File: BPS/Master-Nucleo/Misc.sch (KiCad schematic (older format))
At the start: 34 parts, among them J11 FrontFans, J12 BackFans, J13 ErrorLightConnector, Q3 NTR4003NT1G, Q4 NTR4003NT1G, U16 SI8261ABC-IS

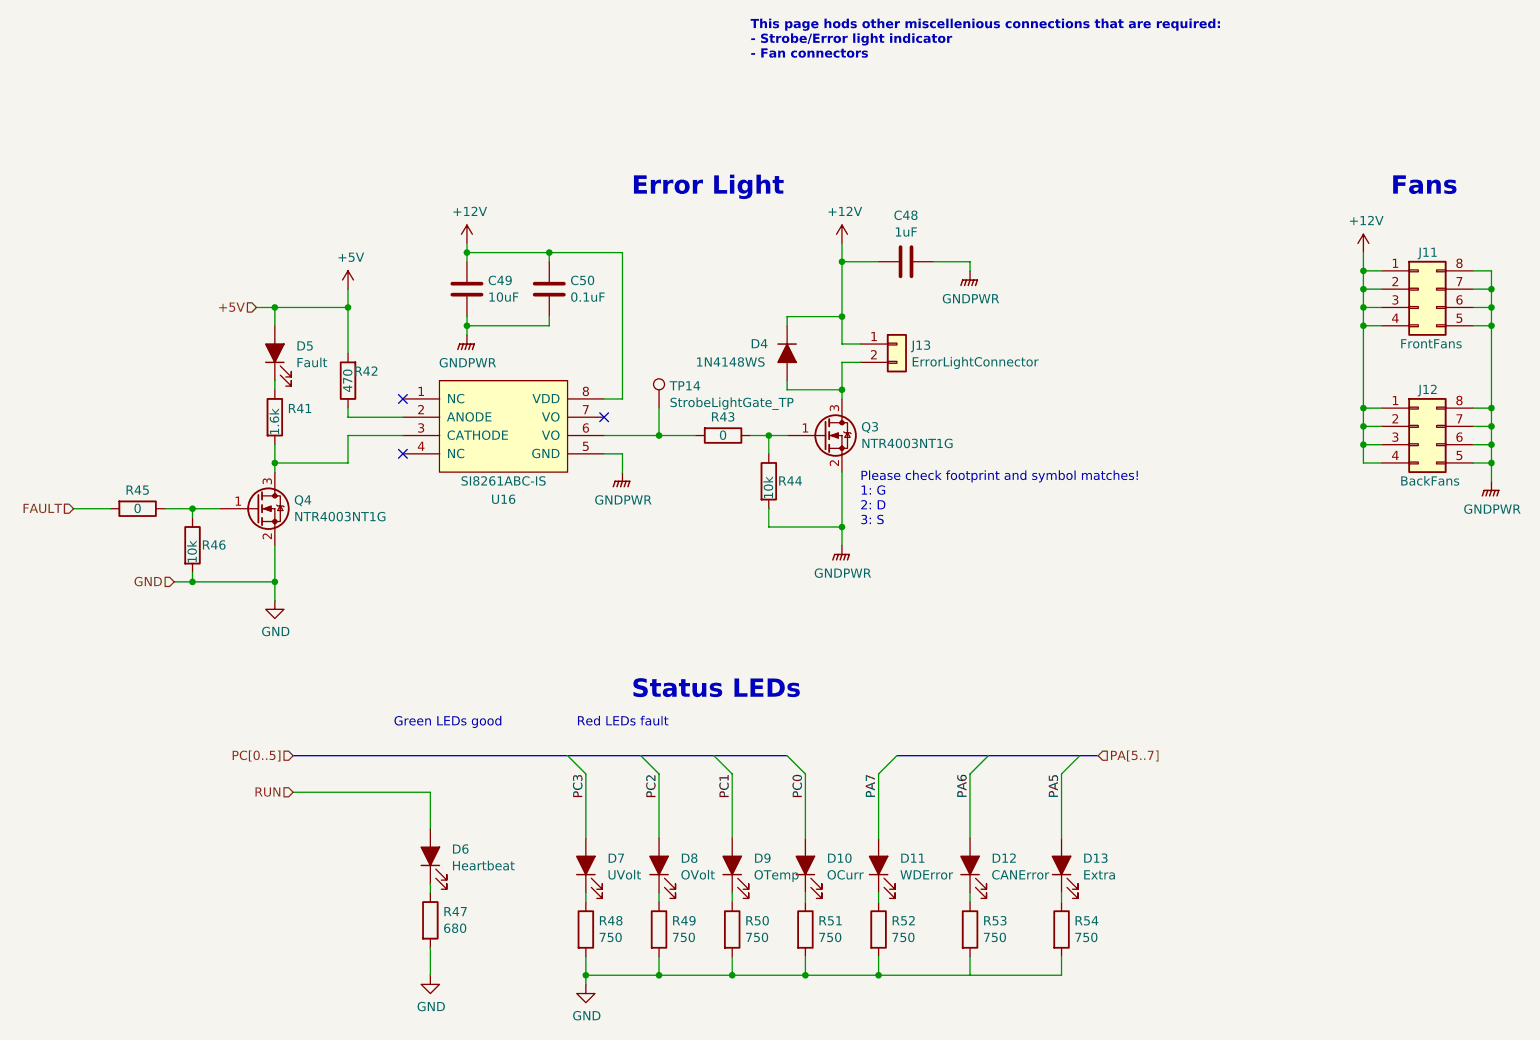
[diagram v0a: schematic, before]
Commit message: Adds Nucleo version of master board.
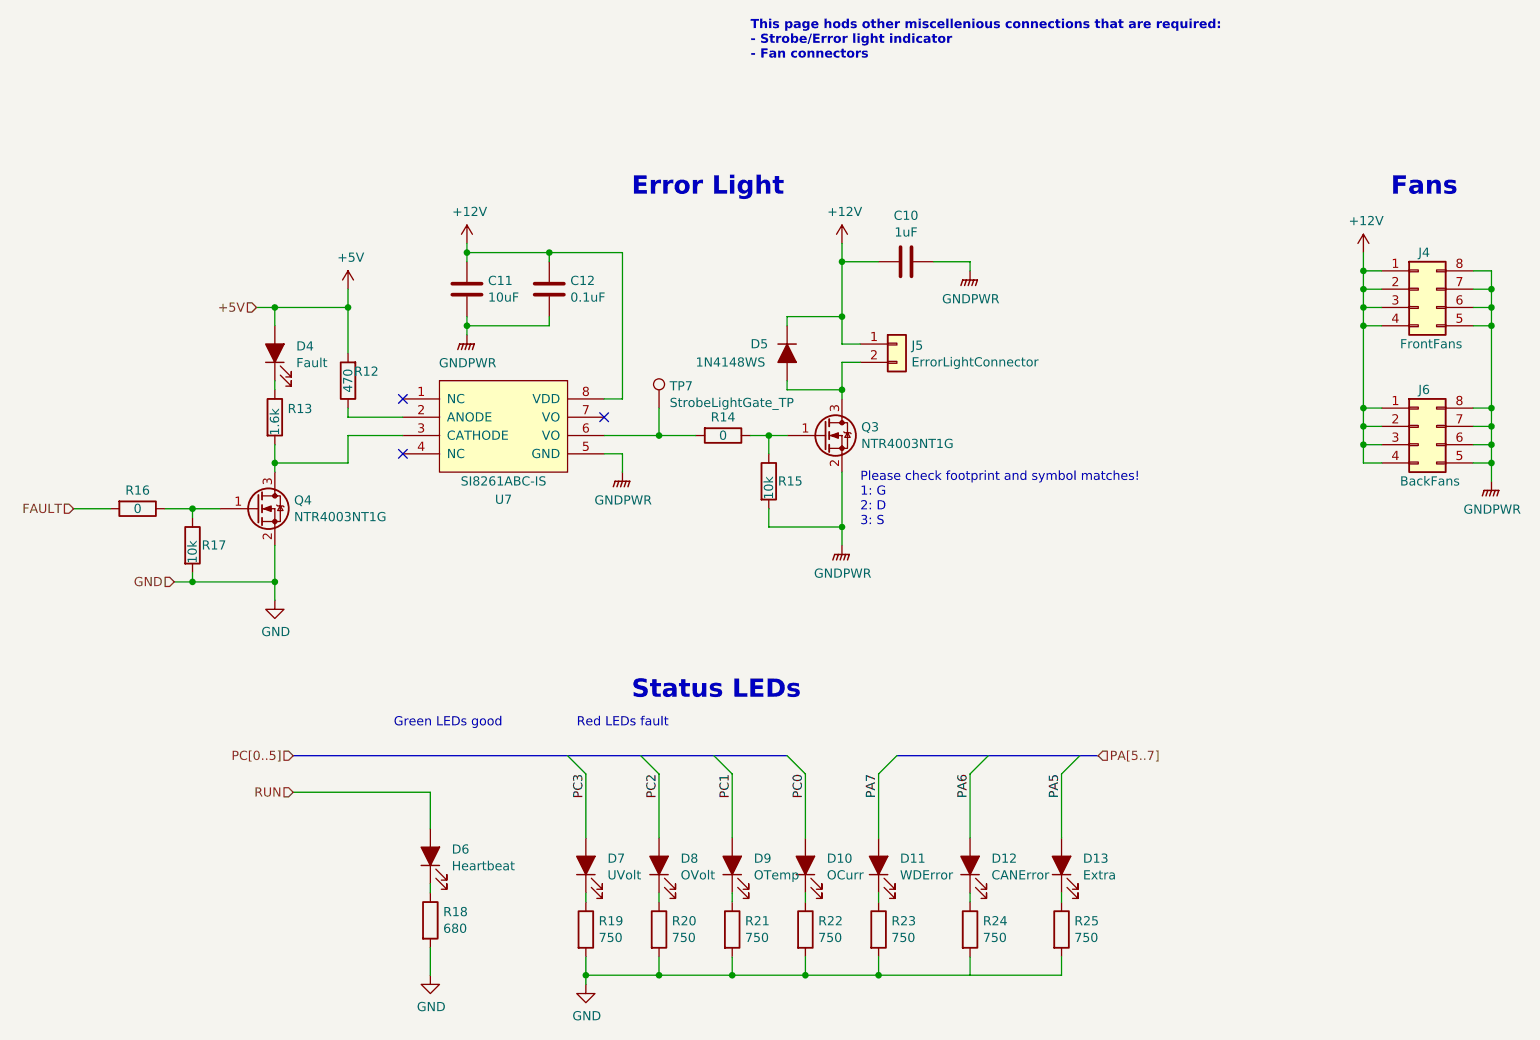
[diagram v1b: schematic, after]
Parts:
- renumbered C49 to C11, C50 to C12, J11 to J4, J13 to J5, J12 to J6, R42 to R12, R47 to R18, R48 to R19, R49 to R20, R50 to R21, R51 to R22, R52 to R23, R53 to R24, R54 to R25, U16 to U7
